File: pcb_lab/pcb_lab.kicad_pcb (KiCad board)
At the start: 2 copper layers, 1 part

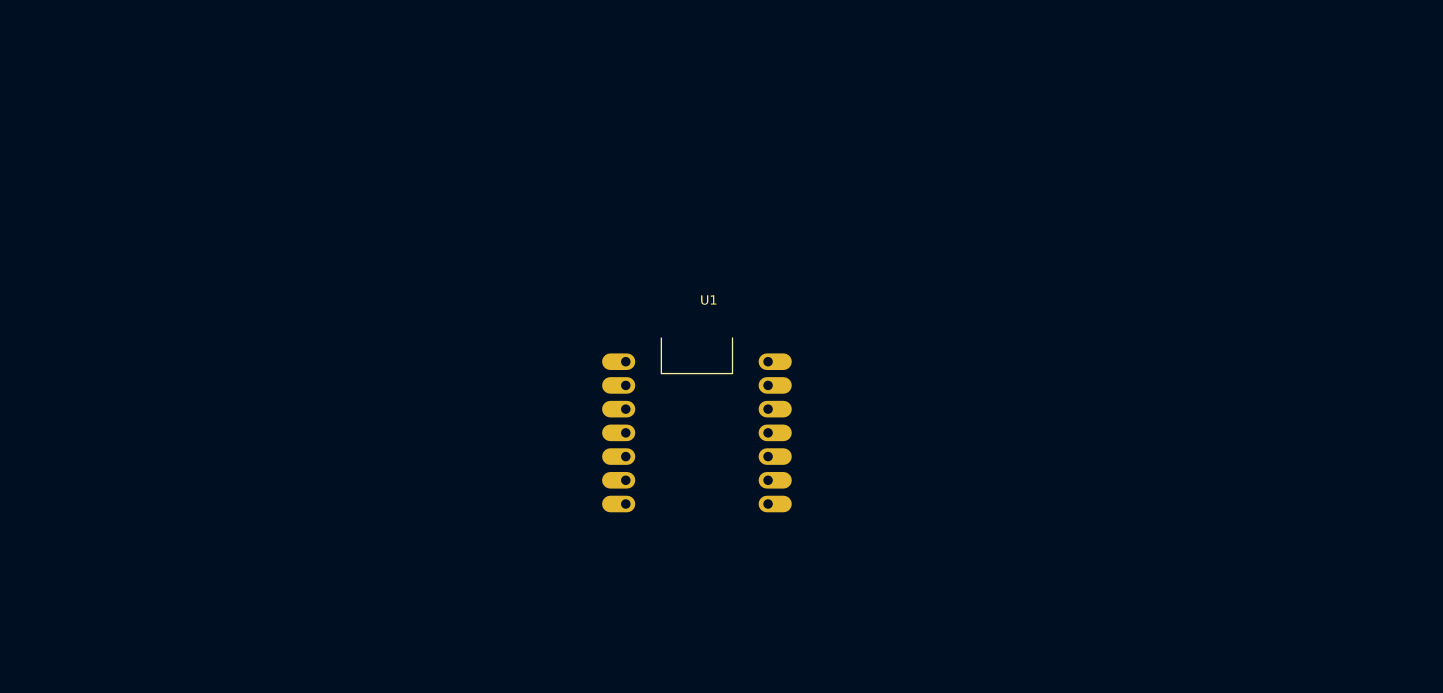
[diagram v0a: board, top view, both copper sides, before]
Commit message: update with battery estimate
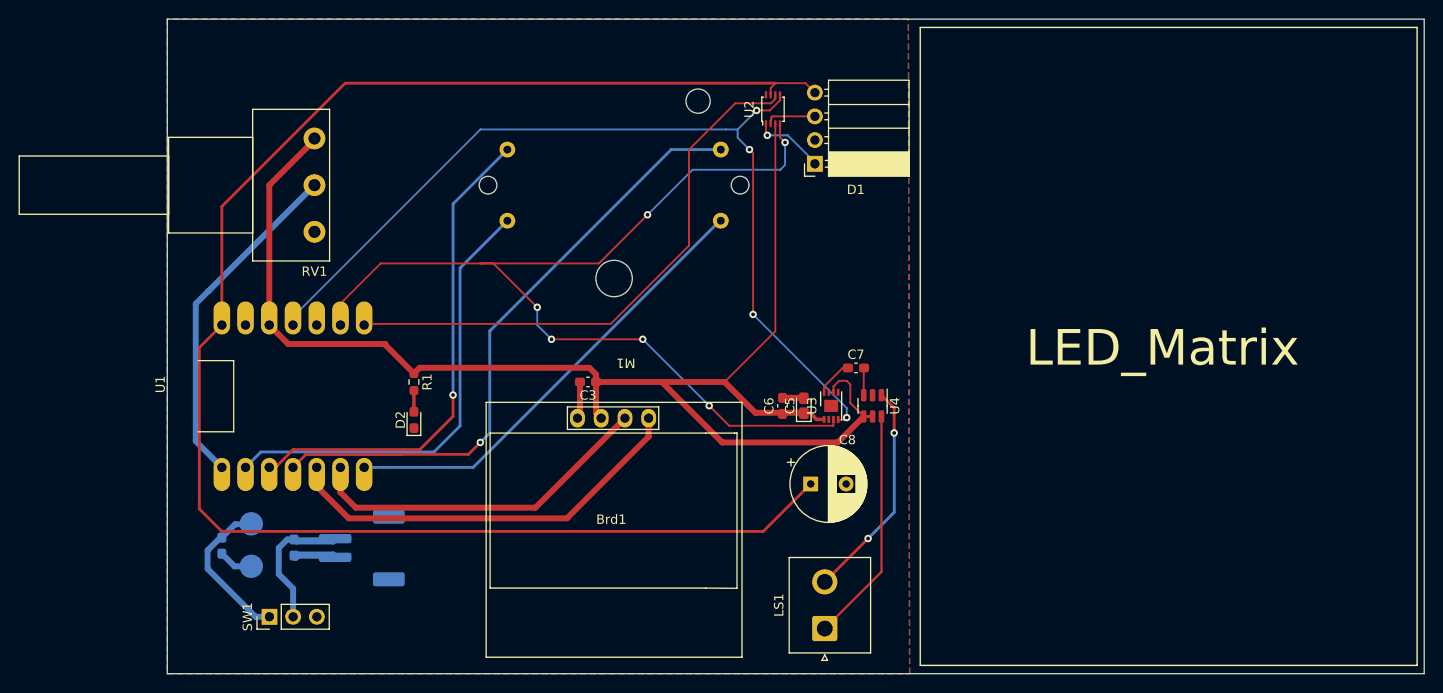
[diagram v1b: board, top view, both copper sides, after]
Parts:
- added Brd1: SSD1306, Library:128x64OLED, F.Cu at (130.5, 108.1)
- added C1: 1u, Capacitor_SMD:C_0603_1608Metric_Pad1.08x0.95mm_HandSolder, B.Cu at (96.5, 111.3)
- added C2: 100n, Capacitor_SMD:C_0603_1608Metric_Pad1.08x0.95mm_HandSolder, B.Cu at (88.8, 111.1)
- added C3: 100n, Capacitor_SMD:C_0603_1608Metric_Pad1.08x0.95mm_HandSolder, F.Cu at (128.0, 93.6)
- added C5: 10u, Capacitor_Tantalum_SMD:CP_EIA-1608-08_AVX-J_Pad1.25x1.05mm_HandSolder, F.Cu at (151.1, 96.2)
- added C6: 100n, Capacitor_SMD:C_0603_1608Metric_Pad1.08x0.95mm_HandSolder, F.Cu at (148.9, 96.2)
- added C7: 100n, Capacitor_SMD:C_0603_1608Metric_Pad1.08x0.95mm_HandSolder, F.Cu at (156.7, 92.1)
- added C8: 220u, Capacitor_THT:CP_Radial_D8.0mm_P3.80mm, F.Cu at (151.9, 104.5)
- added D1: ~, Connector_PinSocket_2.54mm:PinSocket_1x04_P2.54mm_Horizontal, F.Cu at (152.3, 70.2)
- added D2: LED, LED_SMD:LED_0603_1608Metric_Pad1.05x0.95mm_HandSolder, F.Cu at (109.4, 97.7)
- added J1: Battery, Connector_JST:JST_PH_S2B-PH-SM4-TB_1x02-1MP_P2.00mm_Horizontal, B.Cu at (103.8, 111.4)
- added J2: Battery+, TestPoint:TestPoint_Pad_D2.5mm, B.Cu at (92.0, 108.8)
- added J3: Battery-, TestPoint:TestPoint_Pad_D2.5mm, B.Cu at (92.0, 113.4)
- added LS1: Speaker, Connector_JST:JST_NV_B02P-NV_1x02_P5.00mm_Vertical, F.Cu at (153.4, 120.0)
- added M1: Stepper_Motor_bipolar, Library:X27_stepper_motor, F.Cu at (128.3, 62.4)
- added R1: 1k, Resistor_SMD:R_0603_1608Metric_Pad0.98x0.95mm_HandSolder, F.Cu at (109.4, 93.6)
- added RV1: R_Potentiometer, Potentiometer_THT:Potentiometer_Piher_PC-16_Single_Horizontal, F.Cu at (98.7, 67.5)
- added SW1: SW_SPDT, Connector_PinHeader_2.54mm:PinHeader_1x03_P2.54mm_Vertical, F.Cu at (93.9, 118.8)
- added U2: TXB0102DCU, Package_SO:VSSOP-8_2.4x2.1mm_P0.5mm, F.Cu at (147.8, 64.4)
- added U3: MCP4921, Package_DFN_QFN:DFN-8-1EP_3x2mm_P0.5mm_EP1.3x1.5mm, F.Cu at (154.1, 96.2)
- added U4: PAM8301, Package_TO_SOT_SMD:SOT-23-6, F.Cu at (158.5, 96.2)
- U1: footprint ESP32:XIAO_ESP32_SENSE -> Library:XIAO_ESP32_SENSE
- moved U1 43.4 mm to (96.4, 95.1), turned to 90 degrees
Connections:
- U1 pad 1: unconnected-(U1-GPIO1_A0_D0-Pad1) -> /Volumn
- U1 pad 10: unconnected-(U1-3V3-Pad10) -> +3.3V
- U1 pad 11: unconnected-(U1-GPIO9_A10_D10_COPI-Pad11) -> /SDI
- U1 pad 13: unconnected-(U1-GPIO7_A8_D8_SCK-Pad13) -> /SCK
- U1 pad 14: unconnected-(U1-GPIO44_D7_RX-Pad14) -> /CS
- U1 pad 2: unconnected-(U1-GPIO2_A1_D1-Pad2) -> /M1
- U1 pad 3: unconnected-(U1-GPIO3_A2_D2-Pad3) -> /M2
- U1 pad 4: unconnected-(U1-GPIO4_A3_D3-Pad4) -> /M3
- U1 pad 5: unconnected-(U1-GPIO4_A3_D3_SDA-Pad5) -> /SDA
- U1 pad 6: unconnected-(U1-GPIO6_A5_D5_SCL-Pad6) -> /SCL
- U1 pad 7: unconnected-(U1-GPIO43_TX_D6-Pad7) -> /M4
- U1 pad 8: unconnected-(U1-5V-Pad8) -> +5V
- U1 pad 9: unconnected-(U1-GND-Pad9) -> GND
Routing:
- net +5V: track 0.00 -> 172.8 mm
- net +3.3V: track 0.00 -> 154.4 mm
- net /SCK: track 0.00 -> 107.5 mm, vias 0 -> 6
- net /SDI: track 0.00 -> 100.0 mm, vias 0 -> 4
- net /M3: track 0.00 -> 66.3 mm, vias 0 -> 1
- net /CS: track 0.00 -> 60.6 mm
- net /M2: track 0.00 -> 53.9 mm, vias 0 -> 1
- net /M1: track 0.00 -> 49.8 mm
- net /M4: track 0.00 -> 49.1 mm
- net /SDA: track 0.00 -> 44.6 mm
- net /SCL: track 0.00 -> 37.8 mm
- net /Volumn: track 0.00 -> 36.7 mm
- net Net-(U4-OUT+): track 0.00 -> 25.4 mm
- net Net-(U4-OUT-): track 0.00 -> 23.6 mm, vias 0 -> 2
- net GND: track 0.00 -> 20.1 mm
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- added copper zone on B.Cu, net GND
- added copper zone on F.Cu, net GND
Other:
- board outline added: 134.6 x 70.1 mm
- board text added: "LED_Matrix"
